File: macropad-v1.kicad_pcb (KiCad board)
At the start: 2 copper layers, 72.2 x 38.1 mm, 24 parts, among them SW1 SW_Push, U1 ATmega32U4-AU, Y1 16MHz

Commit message: usb c v1
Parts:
- removed USB1: Molex-0548190589, random-keyboard-parts:Molex-0548190589
- added D5: PRTR5V0U2X, Package_TO_SOT_SMD:SOT-143, B.Cu at (65.9, 87.3)
- added J1: USB_C_Receptacle_USB2.0, Connector_USB:USB_C_Receptacle_Amphenol_12401548E4-2A, B.Cu at (80.2, 88.1)
- added R5: 5.1k, Resistor_SMD:R_0805_2012Metric, B.Cu at (72.2, 85.7)
- added R6: 5.1k, Resistor_SMD:R_0805_2012Metric, B.Cu at (72.2, 88.1)
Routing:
- net Net-(J1-PadA5): track 0.00 -> 19.2 mm, vias 0 -> 2
- net GND: track 126.6 -> 141.0 mm
- net VCC: track 9.24 -> 19.0 mm, vias 0 -> 2
- net D-: track 39.8 -> 49.5 mm, vias 0 -> 1
- net Net-(J1-PadB5): track 0.00 -> 9.58 mm, vias 0 -> 1
- net Net-(D5-Pad1): track 0.00 -> 8.64 mm, vias 0 -> 2
- net D+: track 41.1 -> 49.0 mm

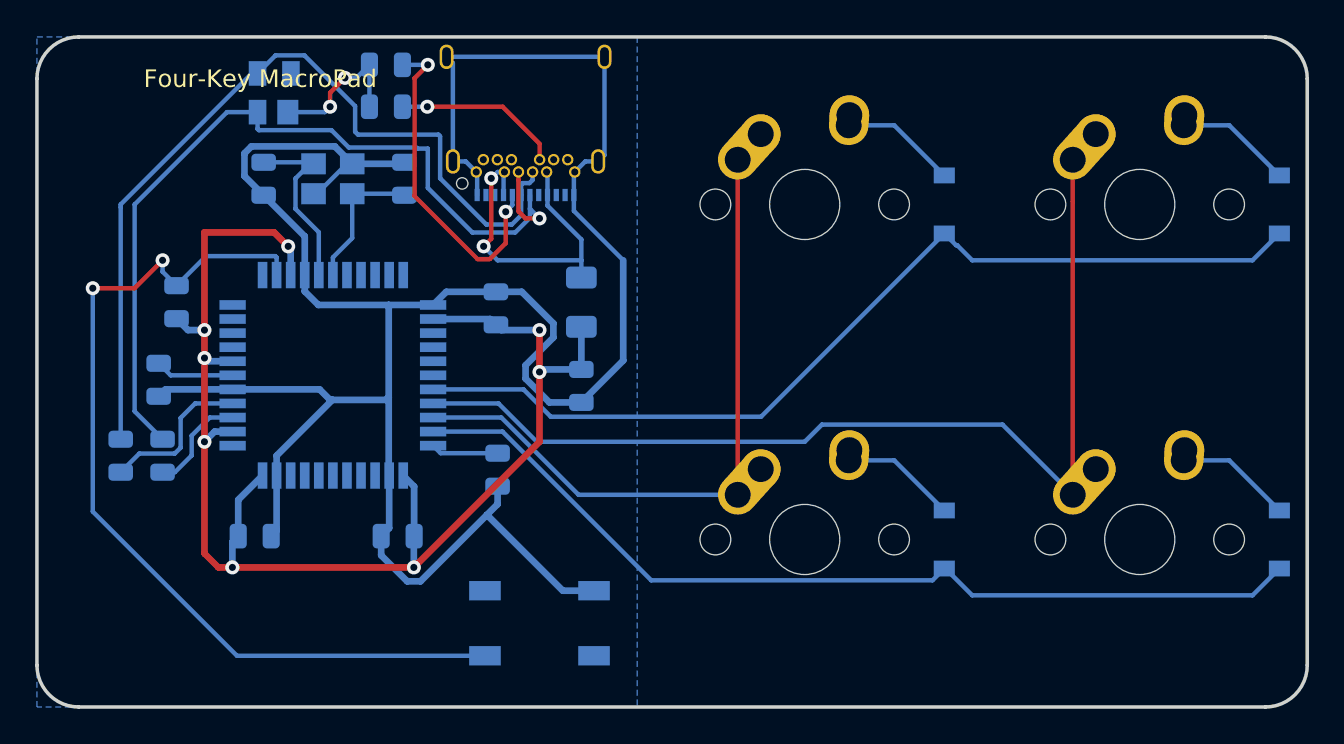
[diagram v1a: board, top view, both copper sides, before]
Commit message: usb c and better routing
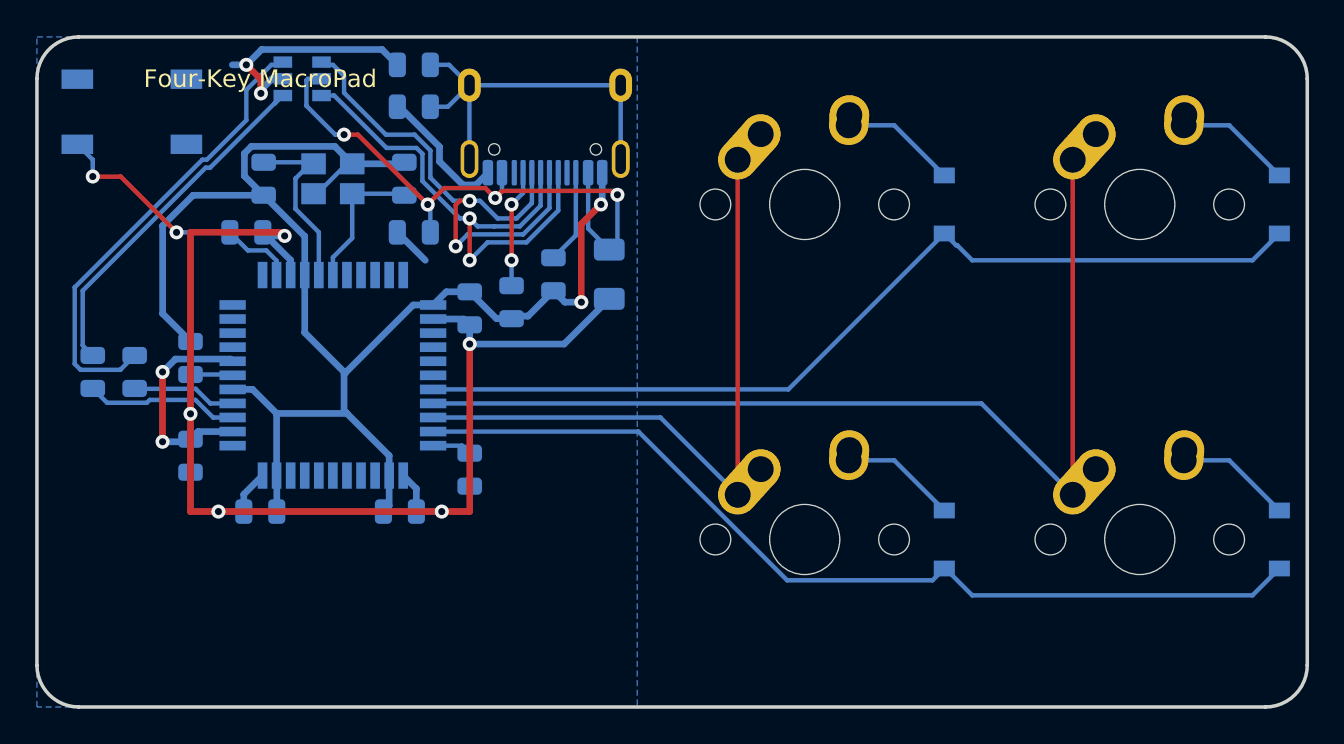
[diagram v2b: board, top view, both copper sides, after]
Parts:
- removed D5: PRTR5V0U2X, Package_TO_SOT_SMD:SOT-143
- added C8: 0.1uF, Capacitor_SMD:C_0805_2012Metric, B.Cu at (73.8, 95.2)
- added C9: 4.7nF, Capacitor_SMD:C_0805_2012Metric, B.Cu at (73.8, 88.1)
- added R7: 1M, Resistor_SMD:R_0805_2012Metric, B.Cu at (73.8, 85.7)
- added U2: USBLC6-2SC6, Package_TO_SOT_SMD:SOT-23-6, B.Cu at (67.5, 86.5)
- J1: value USB_C_Receptacle_USB2.0 -> TYPE-C-31-M12_13; footprint Connector_USB:USB_C_Receptacle_Amphenol_12401548E4-2A -> acheron_Connectors:TYPE-C-31-M-12
- moved SW1 37.2 mm to (57.8, 88.4)
- moved C7 22.6 mm to (61.1, 108.0)
- moved R5 15.3 mm to (79.4, 99.2), turned to 90 degrees
- moved R6 13.5 mm to (81.8, 97.6), turned to 90 degrees
- moved R3 6.20 mm to (55.6, 103.2)
- moved R1 5.61 mm to (64.3, 95.2), turned to 180 degrees
- moved R2 4.83 mm to (57.9, 103.2)
- moved J1 4.61 mm to (81.3, 92.6)
- moved F1 2.25 mm to (84.9, 97.6)
- moved C3 2.19 mm to (61.1, 102.4), turned to 90 degrees
- moved R4 1.59 mm to (77.0, 108.7)
- moved C5 1.49 mm to (77.0, 99.6)
- moved C6 1.43 mm to (65.1, 111.1)
- moved C4 1.40 mm to (73.0, 111.1)
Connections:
- F1 pad 2: VCC -> VBUS
- J1 pad A4: VCC -> VBUS
- J1 pad A6: D+ -> DBus-
- J1 pad A7: D- -> DBus+
- J1 pad B4: VCC -> VBUS
- J1 pad B6: D+ -> DBus-
- J1 pad B7: D- -> DBus+
- R5 pad 1: Net-(D5-Pad1) -> GND
- R6 pad 1: Net-(D5-Pad1) -> GND
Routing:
- net Net-(R1-Pad2): track 52.2 -> 15.6 mm
- net VBUS: track 0.00 -> 35.8 mm, vias 0 -> 4
- net DBus+: track 0.00 -> 31.8 mm, vias 0 -> 2
- net DBus-: track 0.00 -> 30.6 mm, vias 0 -> 2
- net D-: track 49.5 -> 19.9 mm, vias 1 -> 0
- net GND: track 141.0 -> 112.8 mm, vias 0 -> 4
- net Net-(C9-Pad1): track 0.00 -> 23.3 mm
- net D+: track 49.0 -> 26.4 mm
- net VCC: track 19.0 -> 0.00 mm, vias 2 -> 0
- net Net-(J1-PadA5): track 19.2 -> 7.24 mm
- net Net-(D5-Pad1): track 8.64 -> 0.00 mm, vias 2 -> 0
- net Net-(J1-PadB5): track 9.58 -> 5.91 mm, vias 1 -> 0
- net +5V: track 81.7 -> 85.1 mm, vias 8 -> 7
- net Net-(R2-Pad1): track 8.97 -> 5.92 mm
- net Net-(R3-Pad1): track 5.93 -> 8.77 mm
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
